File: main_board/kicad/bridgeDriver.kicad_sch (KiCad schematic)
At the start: 16 parts, among them U9 IR2133

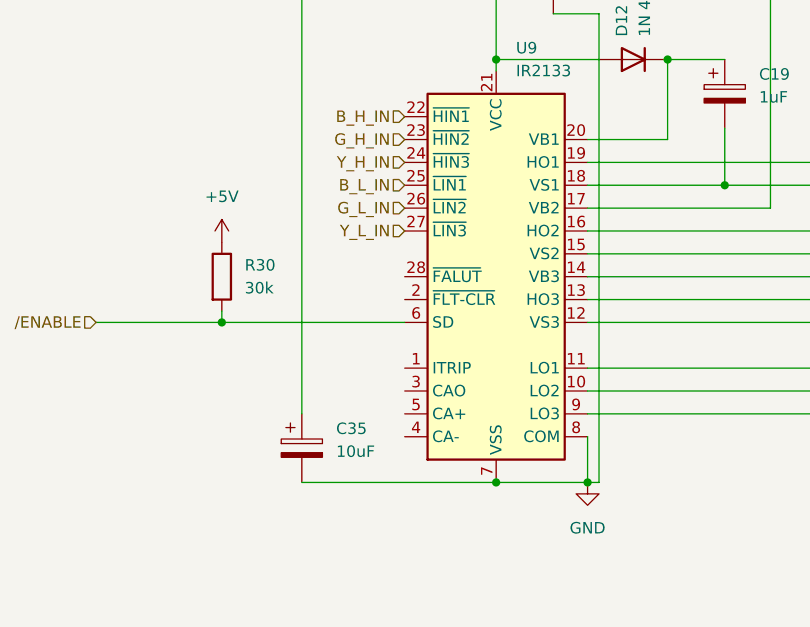
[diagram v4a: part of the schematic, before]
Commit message: resolved ERC
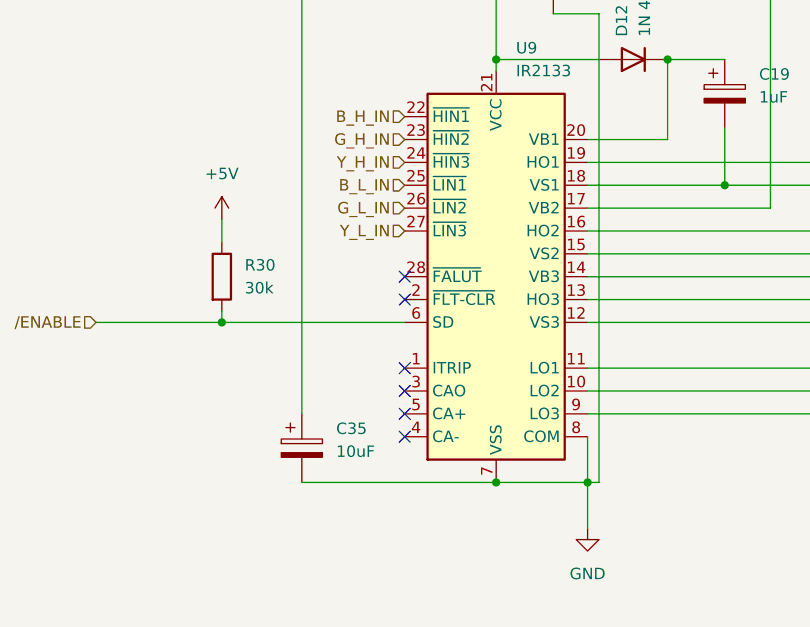
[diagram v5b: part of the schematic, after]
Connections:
- no-connect marks 0 -> 6
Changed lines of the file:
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@@
   (junction (at 163.83 63.5) (diameter 0) (color 0 0 0 0)
   )
+  (no_connect (at 123.19 107.95))
+  (no_connect (at 123.19 123.19))
+  (no_connect (at 123.19 115.57))
+  (no_connect (at 123.19 118.11))
+  (no_connect (at 123.19 120.65))
+  (no_connect (at 123.19 105.41))
   (wire (pts (xy 181.61 133.35) (xy 195.58 133.35))
     (stroke (width 0) (type default))
@@
     (stroke (width 0) (type default))
   )
+  (wire (pts (xy 143.51 128.27) (xy 143.51 133.35))
+    (stroke (width 0) (type default))
+  )
   (wire (pts (xy 181.61 110.49) (xy 203.2 110.49))
     (stroke (width 0) (type default))
@@
     (stroke (width 0) (type default))
   )
+  (wire (pts (xy 111.76 63.5) (xy 111.76 120.65))
+    (stroke (width 0) (type default))
+  )
   (wire (pts (xy 175.26 105.41) (xy 175.26 45.72))
     (stroke (width 0) (type default))
@@
     (stroke (width 0) (type default))
   )
-  (wire (pts (xy 111.76 63.5) (xy 111.76 120.65))
-    (stroke (width 0) (type default))
-  )
   (wire (pts (xy 143.51 123.19) (xy 143.51 128.27))
     (stroke (width 0) (type default))
@@
   )
   (wire (pts (xy 189.23 100.33) (xy 189.23 72.39))
+    (stroke (width 0) (type default))
+  )
+  (wire (pts (xy 102.87 99.06) (xy 102.87 101.6))
     (stroke (width 0) (type default))
   )
@@
     )
   )
-  (symbol (lib_id "power:GND") (at 143.51 128.27 0) (unit 1)
-    (in_bom yes) (on_board yes) (dnp no) (fields_autoplaced)
-    (property "Reference" "#PWR064" (at 143.51 134.62 0)
-      (effects (font (size 1.27 1.27)) hide)
-    )
-    (property "Value" "GND" (at 143.51 133.35 0)
-      (effects (font (size 1.27 1.27)))
-    )
-    (property "Footprint" "" (at 143.51 128.27 0)
-      (effects (font (size 1.27 1.27)) hide)
-    )
-    (property "Datasheet" "" (at 143.51 128.27 0)
+  (symbol (lib_id "power:GND") (at 143.51 133.35 0) (unit 1)
+    (in_bom yes) (on_board yes) (dnp no) (fields_autoplaced)
+    (property "Reference" "#PWR064" (at 143.51 139.7 0)
+      (effects (font (size 1.27 1.27)) hide)
+    )
+    (property "Value" "GND" (at 143.51 138.43 0)
+      (effects (font (size 1.27 1.27)))
+    )
+    (property "Footprint" "" (at 143.51 133.35 0)
+      (effects (font (size 1.27 1.27)) hide)
+    )
+    (property "Datasheet" "" (at 143.51 133.35 0)
       (effects (font (size 1.27 1.27)) hide)
     )
@@
     )
   )
+  (symbol (lib_id "power:+5V") (at 102.87 99.06 0) (unit 1)
+    (in_bom yes) (on_board yes) (dnp no) (fields_autoplaced)
+    (property "Reference" "#PWR053" (at 102.87 102.87 0)
+      (effects (font (size 1.27 1.27)) hide)
+    )
+    (property "Value" "+5V" (at 102.87 93.98 0)
+      (effects (font (size 1.27 1.27)))
+    )
+    (property "Footprint" "" (at 102.87 99.06 0)
+      (effects (font (size 1.27 1.27)) hide)
+    )
+    (property "Datasheet" "" (at 102.87 99.06 0)
+      (effects (font (size 1.27 1.27)) hide)
+    )
+    (pin "1")
+    (instances
+      (project "main"
+        (path "/9139d8e7-a5dc-421f-9a12-f77d83384a16/bd668ffa-15ac-402b-b975-3545159b9a29/a16a43cc-091f-454c-bc41-f84655bef65e"
+          (reference "#PWR053") (unit 1)
+        )
+        (path "/9139d8e7-a5dc-421f-9a12-f77d83384a16/2db218d0-8b01-4da6-8935-13d565fba4cd/a16a43cc-091f-454c-bc41-f84655bef65e"
+          (reference "#PWR021") (unit 1)
+        )
+      )
+    )
+  )
   (symbol (lib_id "Device:C_Polarized") (at 158.75 85.09 0) (unit 1)
     (in_bom yes) (on_board yes) (dnp no) (fields_autoplaced)
@@
         )
       )
-    )
-  )
-  (symbol (lib_id "power:+5V") (at 102.87 101.6 0) (unit 1)
-    (in_bom yes) (on_board yes) (dnp no) (fields_autoplaced)
-    (property "Reference" "#PWR062" (at 102.87 105.41 0)
-      (effects (font (size 1.27 1.27)) hide)
-    )
-    (property "Value" "+5V" (at 102.87 96.52 0)
-      (effects (font (size 1.27 1.27)))
-    )
-    (property "Footprint" "" (at 102.87 101.6 0)
-      (effects (font (size 1.27 1.27)) hide)
-    )
-    (property "Datasheet" "" (at 102.87 101.6 0)
-      (effects (font (size 1.27 1.27)) hide)
-    )
-    (pin "1")
-    (instances
-      (project "main"
-        (path "/9139d8e7-a5dc-421f-9a12-f77d83384a16/bd668ffa-15ac-402b-b975-3545159b9a29/a16a43cc-091f-454c-bc41-f84655bef65e"
-          (reference "#PWR062") (unit 1)
-        )
-        (path "/9139d8e7-a5dc-421f-9a12-f77d83384a16/2db218d0-8b01-4da6-8935-13d565fba4cd/a16a43cc-091f-454c-bc41-f84655bef65e"
-          (reference "#PWR021") (unit 1)
-        )
-      )

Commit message: updated to post review state
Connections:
- net +15V: now also U9.5 (CA+)
- net GND: now also U9.1 (ITRIP), U9.2 (~{FLT-CLR}), U9.4 (CA-)
- no-connect marks 6 -> 2
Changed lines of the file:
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@@
   (junction (at 175.26 45.72) (diameter 0) (color 0 0 0 0)
   )
+  (junction (at 111.76 120.65) (diameter 0) (color 0 0 0 0)
+  )
   (junction (at 158.75 95.25) (diameter 0) (color 0 0 0 0)
   )
@@
   (junction (at 133.35 128.27) (diameter 0) (color 0 0 0 0)
   )
+  (junction (at 120.65 128.27) (diameter 0) (color 0 0 0 0)
+  )
   (junction (at 170.18 102.87) (diameter 0) (color 0 0 0 0)
   )
   (junction (at 102.87 110.49) (diameter 0) (color 0 0 0 0)
   )
+  (junction (at 120.65 115.57) (diameter 0) (color 0 0 0 0)
+  )
   (junction (at 144.78 63.5) (diameter 0) (color 0 0 0 0)
   )
   (junction (at 181.61 110.49) (diameter 0) (color 0 0 0 0)
   )
+  (junction (at 123.19 128.27) (diameter 0) (color 0 0 0 0)
+  )
   (junction (at 143.51 128.27) (diameter 0) (color 0 0 0 0)
   )
   (junction (at 163.83 63.5) (diameter 0) (color 0 0 0 0)
   )
-  (no_connect (at 123.19 107.95))
-  (no_connect (at 123.19 123.19))
-  (no_connect (at 123.19 115.57))
   (no_connect (at 123.19 118.11))
-  (no_connect (at 123.19 120.65))
   (no_connect (at 123.19 105.41))
   (wire (pts (xy 181.61 133.35) (xy 195.58 133.35))
@@
     (stroke (width 0) (type default))
   )
-  (wire (pts (xy 111.76 128.27) (xy 133.35 128.27))
+  (wire (pts (xy 120.65 115.57) (xy 120.65 128.27))
+    (stroke (width 0) (type default))
+  )
+  (wire (pts (xy 111.76 128.27) (xy 120.65 128.27))
     (stroke (width 0) (type default))
   )
@@
     (stroke (width 0) (type default))
   )
+  (wire (pts (xy 123.19 128.27) (xy 133.35 128.27))
+    (stroke (width 0) (type default))
+  )
   (wire (pts (xy 144.78 63.5) (xy 133.35 63.5))
     (stroke (width 0) (type default))
@@
     (stroke (width 0) (type default))
   )
+  (wire (pts (xy 123.19 107.95) (xy 120.65 107.95))
+    (stroke (width 0) (type default))
+  )
   (wire (pts (xy 158.75 88.9) (xy 158.75 95.25))
     (stroke (width 0) (type default))
@@
     (stroke (width 0) (type default))
   )
+  (wire (pts (xy 111.76 120.65) (xy 123.19 120.65))
+    (stroke (width 0) (type default))
+  )
   (wire (pts (xy 143.51 97.79) (xy 163.83 97.79))
     (stroke (width 0) (type default))
@@
     (stroke (width 0) (type default))
   )
+  (wire (pts (xy 120.65 107.95) (xy 120.65 115.57))
+    (stroke (width 0) (type default))
+  )
   (wire (pts (xy 143.51 123.19) (xy 143.51 128.27))
     (stroke (width 0) (type default))
@@
     (stroke (width 0) (type default))
   )
+  (wire (pts (xy 120.65 115.57) (xy 123.19 115.57))
+    (stroke (width 0) (type default))
+  )
   (wire (pts (xy 189.23 100.33) (xy 189.23 72.39))
     (stroke (width 0) (type default))
@@
     (stroke (width 0) (type default))
   )
+  (wire (pts (xy 123.19 123.19) (xy 123.19 128.27))
+    (stroke (width 0) (type default))
+  )
   (wire (pts (xy 107.95 63.5) (xy 111.76 63.5))
     (stroke (width 0) (type default))
@@
     (stroke (width 0) (type default))
   )
+  (wire (pts (xy 120.65 128.27) (xy 123.19 128.27))
+    (stroke (width 0) (type default))
+  )

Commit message: added footprints
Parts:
- C18, C19, C21, C35: footprint (none) -> Capacitor_THT:CP_Radial_D5.0mm_P2.00mm
- C36: footprint (none) -> Capacitor_THT:CP_Radial_D8.0mm_P3.50mm
- D12, D13, D14: footprint (none) -> Diode_THT:D_DO-41_SOD81_P7.62mm_Horizontal
- R30, R31, R32, R33, R34, R35, R36: footprint (none) -> Resistor_THT:R_Axial_DIN0207_L6.3mm_D2.5mm_P7.62mm_Horizontal
- U9: footprint Package_DIP:DIP-28_W15.24mm -> Package_DIP:DIP-28_W15.24mm_Socket_LongPads
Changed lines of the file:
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@@
       (effects (font (size 1.27 1.27)) (justify left))
     )
-    (property "Footprint" "Package_DIP:DIP-28_W15.24mm" (at 133.35 138.43 0)
+    (property "Footprint" "Package_DIP:DIP-28_W15.24mm_Socket_LongPads" (at 133.35 138.43 0)
       (effects (font (size 1.27 1.27)) hide)
     )
@@
       (effects (font (size 1.27 1.27)))
     )
-    (property "Footprint" "" (at 199.39 74.168 90)
+    (property "Footprint" "Resistor_THT:R_Axial_DIN0207_L6.3mm_D2.5mm_P7.62mm_Horizontal" (at 199.39 74.168 90)
       (effects (font (size 1.27 1.27)) hide)
     )
@@
       (effects (font (size 1.27 1.27)))
     )
-    (property "Footprint" "" (at 199.39 66.548 90)
+    (property "Footprint" "Resistor_THT:R_Axial_DIN0207_L6.3mm_D2.5mm_P7.62mm_Horizontal" (at 199.39 66.548 90)
       (effects (font (size 1.27 1.27)) hide)
     )
@@
       (effects (font (size 1.27 1.27)) (justify left))
     )
-    (property "Footprint" "" (at 171.1452 71.12 0)
+    (property "Footprint" "Capacitor_THT:CP_Radial_D5.0mm_P2.00mm" (at 171.1452 71.12 0)
       (effects (font (size 1.27 1.27)) hide)
     )
@@
       (effects (font (size 1.27 1.27)) (justify left))
     )
-    (property "Footprint" "" (at 101.092 105.41 90)
+    (property "Footprint" "Resistor_THT:R_Axial_DIN0207_L6.3mm_D2.5mm_P7.62mm_Horizontal" (at 101.092 105.41 90)
       (effects (font (size 1.27 1.27)) hide)
     )
@@
       (effects (font (size 1.27 1.27)) (justify left))
     )
-    (property "Footprint" "" (at 112.7252 128.27 0)
+    (property "Footprint" "Capacitor_THT:CP_Radial_D5.0mm_P2.00mm" (at 112.7252 128.27 0)
       (effects (font (size 1.27 1.27)) hide)
     )
@@
       (effects (font (size 1.27 1.27)) (justify right))
     )
-    (property "Footprint" "" (at 160.02 63.5 0)
+    (property "Footprint" "Diode_THT:D_DO-41_SOD81_P7.62mm_Horizontal" (at 160.02 63.5 0)
       (effects (font (size 1.27 1.27)) hide)
     )
@@
       (effects (font (size 1.27 1.27)) (justify left))
     )
-    (property "Footprint" "" (at 159.7152 88.9 0)
+    (property "Footprint" "Capacitor_THT:CP_Radial_D5.0mm_P2.00mm" (at 159.7152 88.9 0)
       (effects (font (size 1.27 1.27)) hide)
     )
@@
       (effects (font (size 1.27 1.27)) (justify right))
     )
-    (property "Footprint" "" (at 171.45 45.72 0)
+    (property "Footprint" "Diode_THT:D_DO-41_SOD81_P7.62mm_Horizontal" (at 171.45 45.72 0)
       (effects (font (size 1.27 1.27)) hide)
     )
@@
       (effects (font (size 1.27 1.27)) (justify left))
     )
-    (property "Footprint" "" (at 140.6652 76.2 0)
+    (property "Footprint" "Capacitor_THT:CP_Radial_D8.0mm_P3.50mm" (at 140.6652 76.2 0)
       (effects (font (size 1.27 1.27)) hide)
     )
@@
       (effects (font (size 1.27 1.27)))
     )
-    (property "Footprint" "" (at 199.39 135.128 90)
+    (property "Footprint" "Resistor_THT:R_Axial_DIN0207_L6.3mm_D2.5mm_P7.62mm_Horizontal" (at 199.39 135.128 90)
       (effects (font (size 1.27 1.27)) hide)
     )
@@
       (effects (font (size 1.27 1.27)))
     )
-    (property "Footprint" "" (at 199.39 81.788 90)
+    (property "Footprint" "Resistor_THT:R_Axial_DIN0207_L6.3mm_D2.5mm_P7.62mm_Horizontal" (at 199.39 81.788 90)
       (effects (font (size 1.27 1.27)) hide)
     )
@@
       (effects (font (size 1.27 1.27)) (justify left))
     )
-    (property "Footprint" "" (at 182.5752 53.34 0)
+    (property "Footprint" "Capacitor_THT:CP_Radial_D5.0mm_P2.00mm" (at 182.5752 53.34 0)
       (effects (font (size 1.27 1.27)) hide)
     )
@@
       (effects (font (size 1.27 1.27)))
     )
-    (property "Footprint" "" (at 199.39 142.748 90)
+    (property "Footprint" "Resistor_THT:R_Axial_DIN0207_L6.3mm_D2.5mm_P7.62mm_Horizontal" (at 199.39 142.748 90)
       (effects (font (size 1.27 1.27)) hide)
     )
@@
       (effects (font (size 1.27 1.27)) (justify right))
     )
-    (property "Footprint" "" (at 148.59 81.28 0)
+    (property "Footprint" "Diode_THT:D_DO-41_SOD81_P7.62mm_Horizontal" (at 148.59 81.28 0)
       (effects (font (size 1.27 1.27)) hide)
     )
@@
       (effects (font (size 1.27 1.27)))
     )
-    (property "Footprint" "" (at 199.39 127.508 90)
-      (effects (font (size 1.27 1.27)) hide)
-    )
+    (property "Footprint" "Resistor_THT:R_Axial_DIN0207_L6.3mm_D2.5mm_P7.62mm_Horizontal" (at 199.39 127.508 90)
+      (effects (font (size 1.27 1.27)) hide)
+    )
